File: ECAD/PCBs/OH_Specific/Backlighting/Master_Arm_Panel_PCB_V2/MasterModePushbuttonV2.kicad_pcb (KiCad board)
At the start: 2 copper layers, 45.7 x 123.5 mm, 37 parts, among them J1 BL IN, J2 BL OUT, J3 READY, J4 MASTER MODE, SW1 READY, SW2 A/A, SW3 A/G

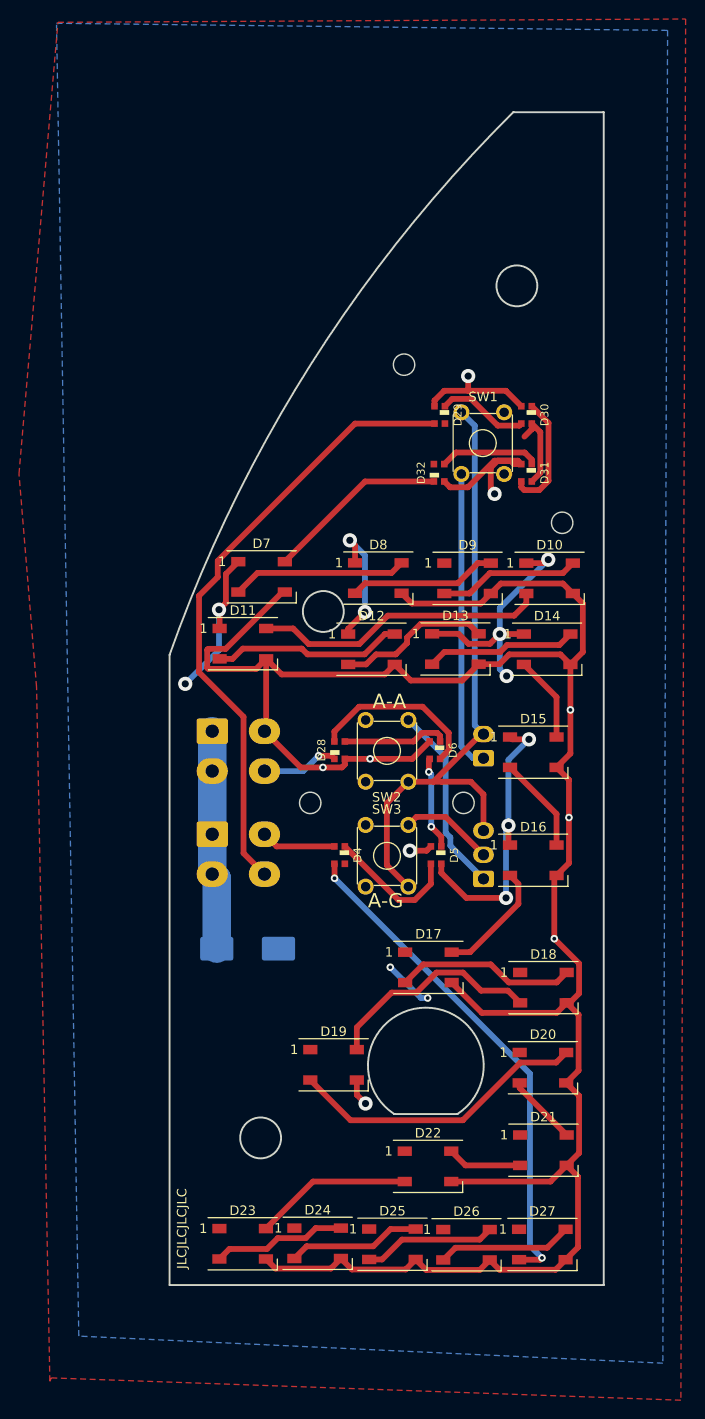
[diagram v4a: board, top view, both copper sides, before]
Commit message: Backlighting PCB KiCad library & Master Arm tweaks
Added - BR10K pot silkscreen symbol
Added - S2AL silkscreen symbol
Added - S3AL silkscreen symbol
Added - 6-32 screw silkscreen symbol
Added - OpenHornet Logo small silkscreen symbol
Added - CC-BY-NC-SA silkscreen symbol
Changed - Master Arm backlighting PCB traces
Added - Silkscreens back to master arm backlighting PCB.
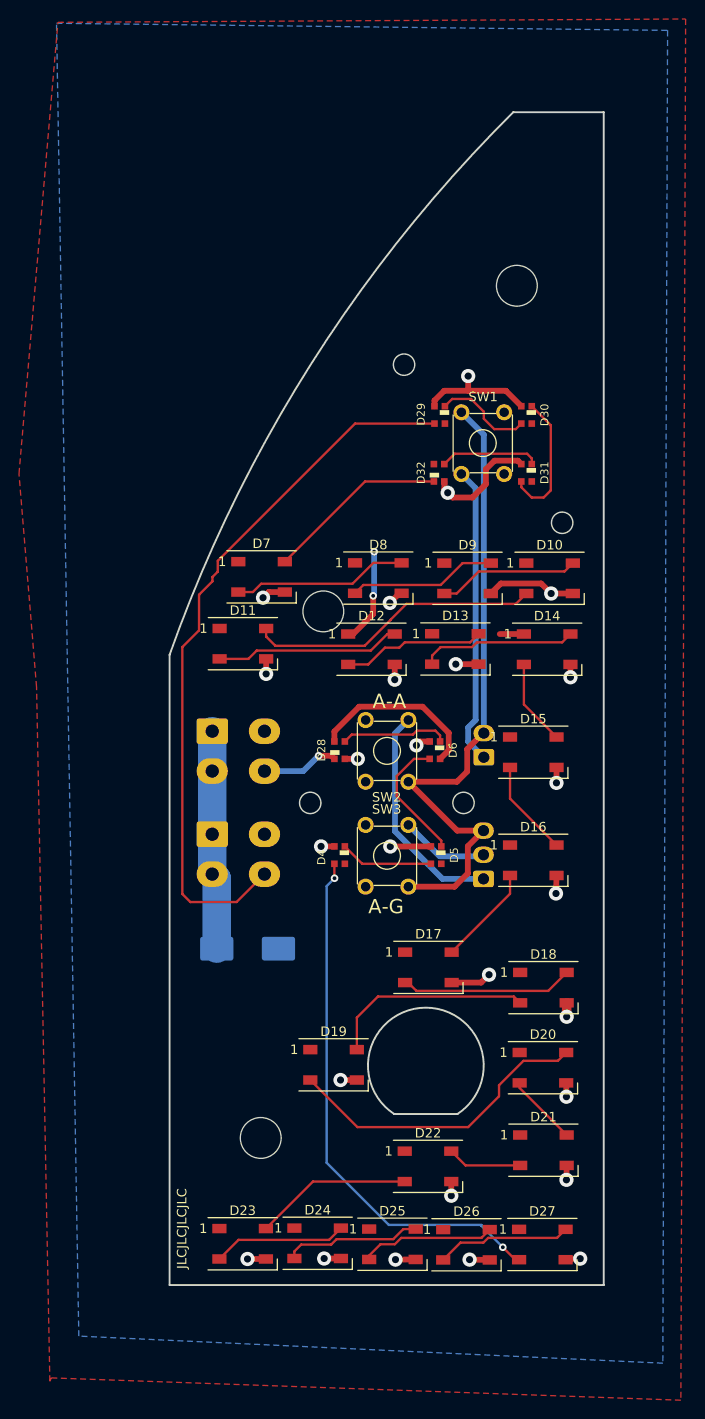
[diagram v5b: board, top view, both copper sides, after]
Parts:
- added H1: OHPanelScrew, OH_Backlighting:OH_Panel_6-32_PHS, F.Cu at (234.9, 47.3)
- added H2: OHPanelScrew, OH_Backlighting:OH_Panel_6-32_PHS, F.Cu at (214.5, 81.6)
- added H3: OHPanelScrew, OH_Backlighting:OH_Panel_6-32_PHS, F.Cu at (207.9, 137.1)
- added LOGO1: CC-BY-NC-SA_Icon, OH_KiCAD_Libraries:CC-BY-NC-SA-Small, B.Cu at (222.8, 72.5)
- added LOGO2: OpenHornetLogoSmall, OH_KiCAD_Libraries:OH_LOGO_37.7mm_5.9mm, B.Cu at (221.9, 146.1)
- added LOGO3: OH_S2AL_Silkscreen, OH_Backlighting:S2AL_Toggle_Silkscreen, F.Cu at (234.4, 129.2)
- moved J3 0.11 mm to (231.4, 97.0)
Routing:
- net /LEDGND: track 284.6 -> 79.3 mm, vias 9 -> 26
- net /LED+5V: track 144.8 -> 54.2 mm, vias 12 -> 2
- net /DATAIN: track 65.5 -> 75.7 mm
- net Net-(D4-Pad1): track 14.2 -> 9.82 mm
- net Net-(D5-Pad1): track 9.80 -> 13.6 mm, vias 2 -> 0
- net /AA_SW: track 20.0 -> 23.7 mm
- net Net-(D27-Pad2): track 53.0 -> 56.4 mm
- net Net-(D16-Pad2): track 12.5 -> 10.6 mm
- net Net-(D30-Pad1): track 12.6 -> 14.2 mm
- net Net-(D18-Pad2): track 23.3 -> 21.8 mm
- net Net-(D19-Pad2): track 31.7 -> 32.9 mm
- net Net-(D12-Pad2): track 16.3 -> 15.1 mm
- net GND: track 67.4 -> 68.3 mm
- net Net-(D17-Pad2): track 19.0 -> 18.2 mm
- net Net-(D29-Pad1): track 9.61 -> 10.4 mm
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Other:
- outline, holes or cut-outs redrawn

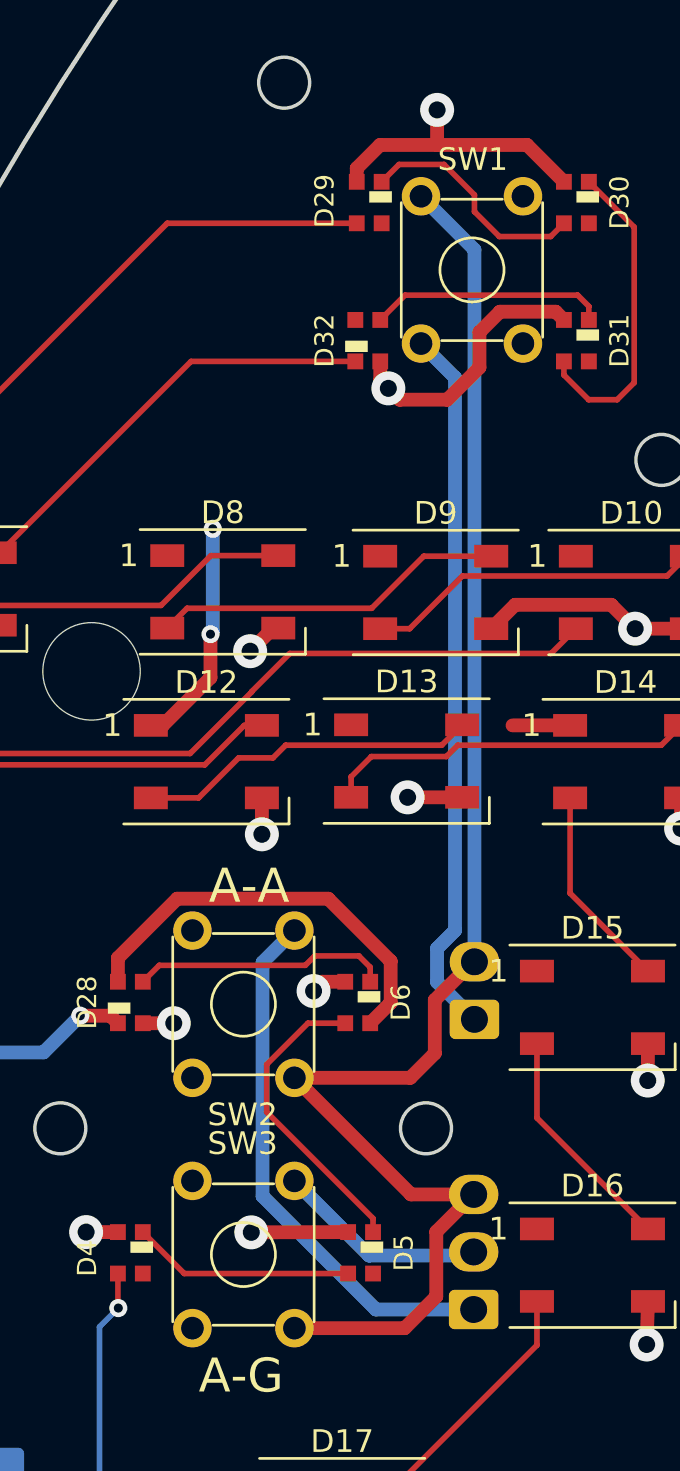
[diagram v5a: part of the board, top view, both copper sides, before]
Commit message: Master Arm Updates
Updated PCB to reroute incorrect traces for switches.
Updated Master Arm spacer to clearance backface PTH components.
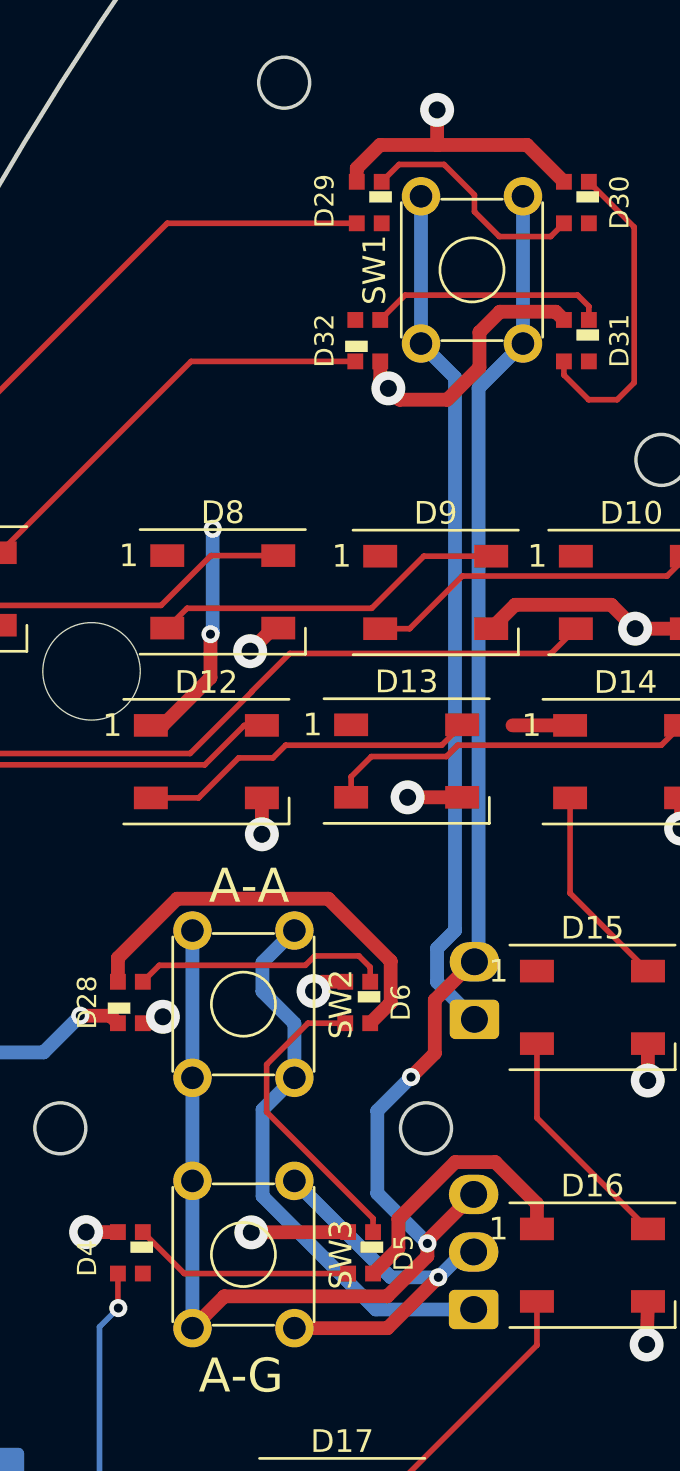
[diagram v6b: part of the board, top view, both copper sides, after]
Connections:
- SW1 pad 2: GND -> /READY_SW
- SW1 pad 3: (no net) -> GND
- SW1 pad 4: (no net) -> GND
- SW2 pad 2: GND -> /AA_SW
- SW2 pad 3: (no net) -> GND
- SW2 pad 4: (no net) -> GND
- SW3 pad 2: GND -> /AG_SW
- SW3 pad 3: (no net) -> GND
- SW3 pad 4: (no net) -> GND
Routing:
- net GND: track 68.3 -> 82.7 mm, vias 0 -> 2
- net /LED+5V: track 54.2 -> 66.1 mm
- net /AG_SW: track 9.34 -> 17.4 mm, vias 0 -> 1
- net /READY_SW: track 31.5 -> 38.0 mm
- net /AA_SW: track 23.7 -> 24.9 mm
